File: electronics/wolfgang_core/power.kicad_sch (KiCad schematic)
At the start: 42 parts, among them J1 Power Supply, J2 Battery, Q1 SUM110P06-08L-E3, Q2 SUM110P06-08L-E3, Q3 SUM110P06-08L-E3, Q4 SUM110P06-08L-E3, U1 LM5001MA, U2 ACS724xLCTR-50AB, U3 LTC4418IUF-PBF

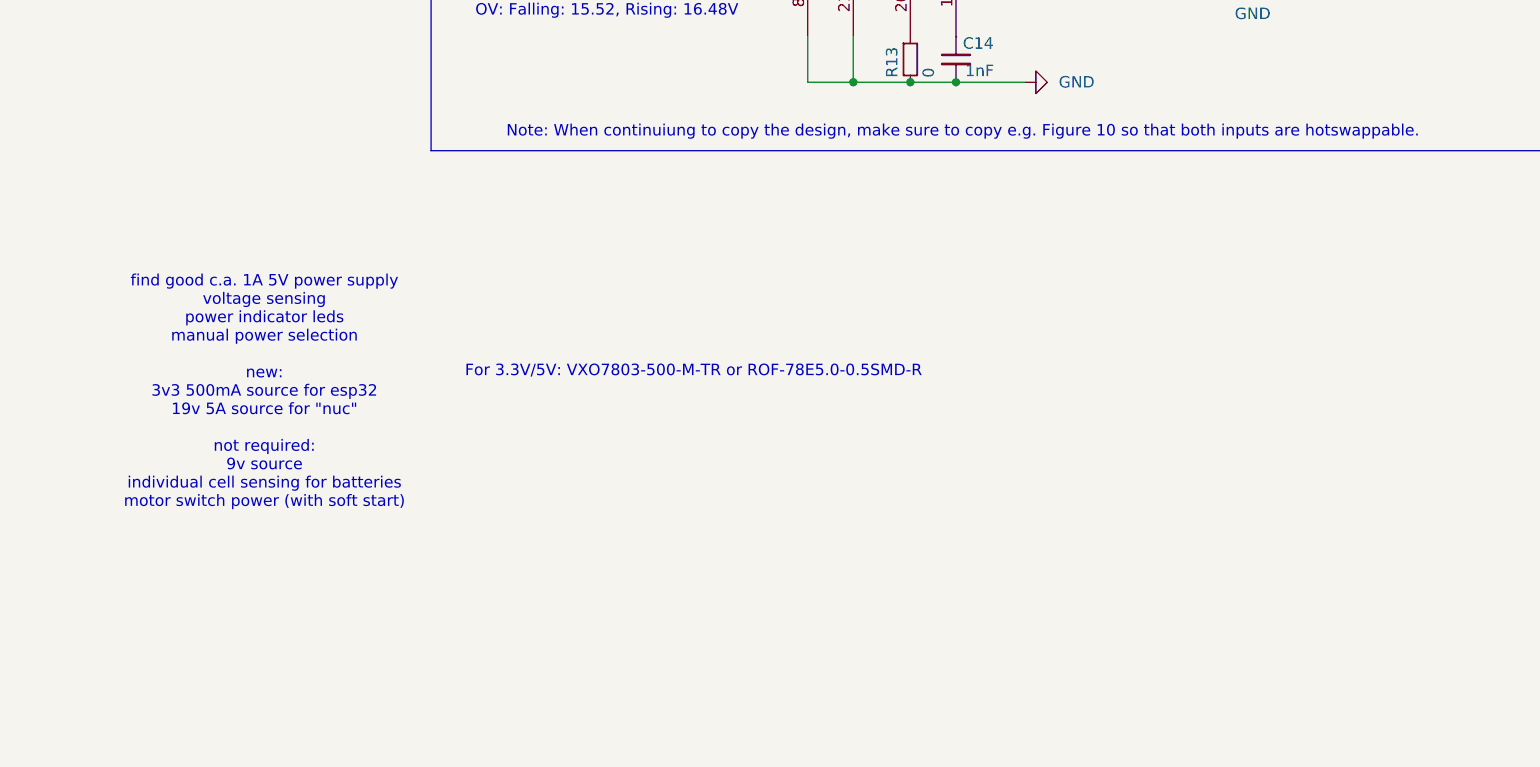
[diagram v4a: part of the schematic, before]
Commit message: Added 5V and 3.3V converters
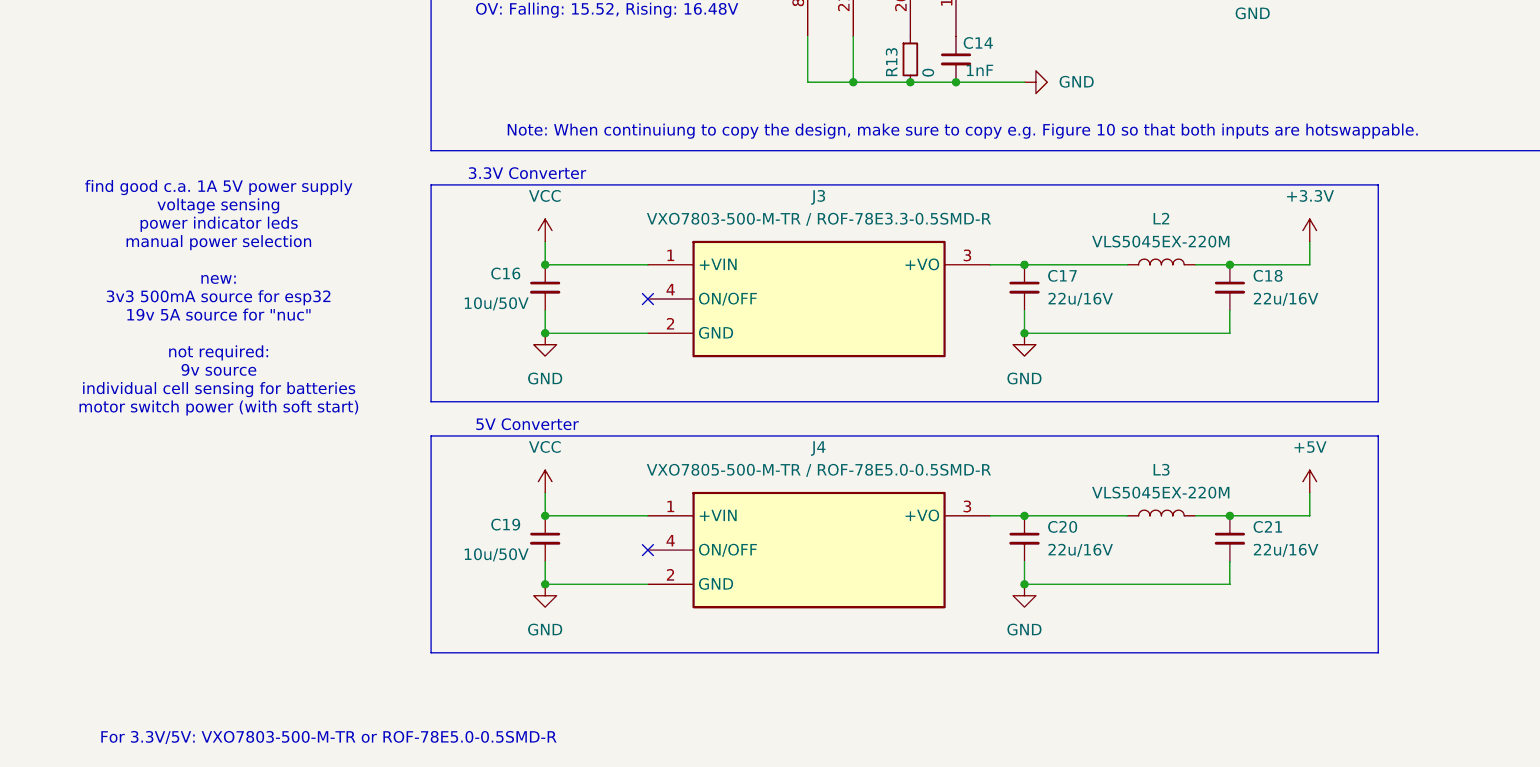
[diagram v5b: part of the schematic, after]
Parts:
- added C16, C19: 10u/50V, symbol Device:C_Small
- added C17, C18, C20, C21: 22u/16V, symbol Device:C_Small
- added J3: VXO7803-500-M-TR / ROF-78E3.3-0.5SMD-R, VXO7803500MTR, symbol VXO7803-500-M-TR:VXO7803-500-M-TR
- added J4: VXO7805-500-M-TR / ROF-78E5.0-0.5SMD-R, VXO7803500MTR, symbol VXO7803-500-M-TR:VXO7803-500-M-TR
- added L2, L3: VLS5045EX-220M, symbol Device:L
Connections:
- net +3.3V: now also C18.1, L2.2
- net +5V: now also C21.1, L3.2
- net GND: now also C16.2, C17.2, C18.2, C19.2, C20.2, C21.2, J3.2 (GND), J4.2 (GND)
- net VCC: now also C16.1, C19.1, J3.1 (+VIN), J4.1 (+VIN)
- new net: C20.1, J4.3 (+VO), L3.1
- new net: C17.1, J3.3 (+VO), L2.1
- no-connect marks 2 -> 4
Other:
- note added: "3.3V Converter"
- note added: "5V Converter"

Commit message: Add Power Switch, Sensing, Indicators
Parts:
- added C23: 0.01uF, symbol Device:C_Small
- added D10: LED RED, symbol Device:LED
- added D11: LED GREEN, symbol Device:LED
- added JP3: bypass uC, symbol Jumper:Jumper_2_Bridged
- added Q5: BSS138P,215, Package_TO_SOT_SMD:SOT-23, symbol Transistor_FET:BSS138
- added Q6: IPD068P03L3GATMA1, symbol Simulation_SPICE:PMOS
- added R14, R18, R21, R23, R25, R27: 10K, symbol Device:R_Small
- added R15: 1K8, symbol Device:R_Small
- added R16: 3K3, symbol Device:R_Small
- added R17: 120, symbol Device:R_Small
- added R19, R29, R30: 4K7, symbol Device:R_Small
- added R20: 100K, symbol Device:R_Small
- added R22, R24, R26, R28: 2K, symbol Device:R_Small
- added SW1: power_switch, symbol Switch:SW_SPDT
- added U4: SN74AHCT1G08, Package_TO_SOT_SMD:SOT-23-5, symbol 74xGxx:74AHCT1G08
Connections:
- net +5V: now also R14.1, R15.1, U4.5 (VCC)
- net GND: now also Q5.2 (S), R16.2, R18.1, R22.2, R24.2, R26.2, R28.2, R29.2, R30.2, SW1.2 (B), U4.3 (GND)
- net VCC: now also D10.2 (A), Q6.3 (S), R19.2, R25.1
- net v_bat: now also R23.1
- net v_ext: now also R21.1
- new net: JP3.2 (B), R15.2, R16.1, U4.2
- new net: Q5.1 (G), R17.2, R18.2
- new net: C23.1, Q6.2 (G), R20.1
- new net: D10.1 (K), R29.1
- new net: Q5.3 (D), R19.1, R20.2
- new net: D11.1 (K), R30.1
- new net VDXL: C23.2, Q6.1 (D)
- new net VXDL: D11.2 (A), R27.1
- new net switch_power: R17.1, U4.4
- new net switch_power_manual: R14.2, SW1.1 (A), U4.1
- new net switch_power_uc: JP3.1 (A)
- new net v_bat_sense: R23.2, R24.1
- new net v_ext_sense: R21.2, R22.1
- new net vcc_sense: R25.2, R26.1
- new net vxdl_sense: R27.2, R28.1
- no-connect marks 4 -> 5
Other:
- note added: "Manual Power Switch"
- note added: "Motor Power Manual/uc selection"
- note added: "Motor Power Switch"
- note added: "Power Indicator LEDs"
- note added: "Voltage Sensing"
- note added: "power indicator leds new: 3v3 500mA source for esp32 19v 5A source for "nuc" not required: 9v source individual cell sensing for batteries"
- note removed: "For 3.3V/5V: VXO7803-500-M-TR or ROF-78E5.0-0.5SMD-R"
- note removed: "find good c.a. 1A 5V power supply voltage sensing power indicator leds manual power selection new: 3v3 500mA source for esp32 19v 5A source for "nuc" not required: 9v source individual cell sensing for batteries motor switch power (with soft start)"

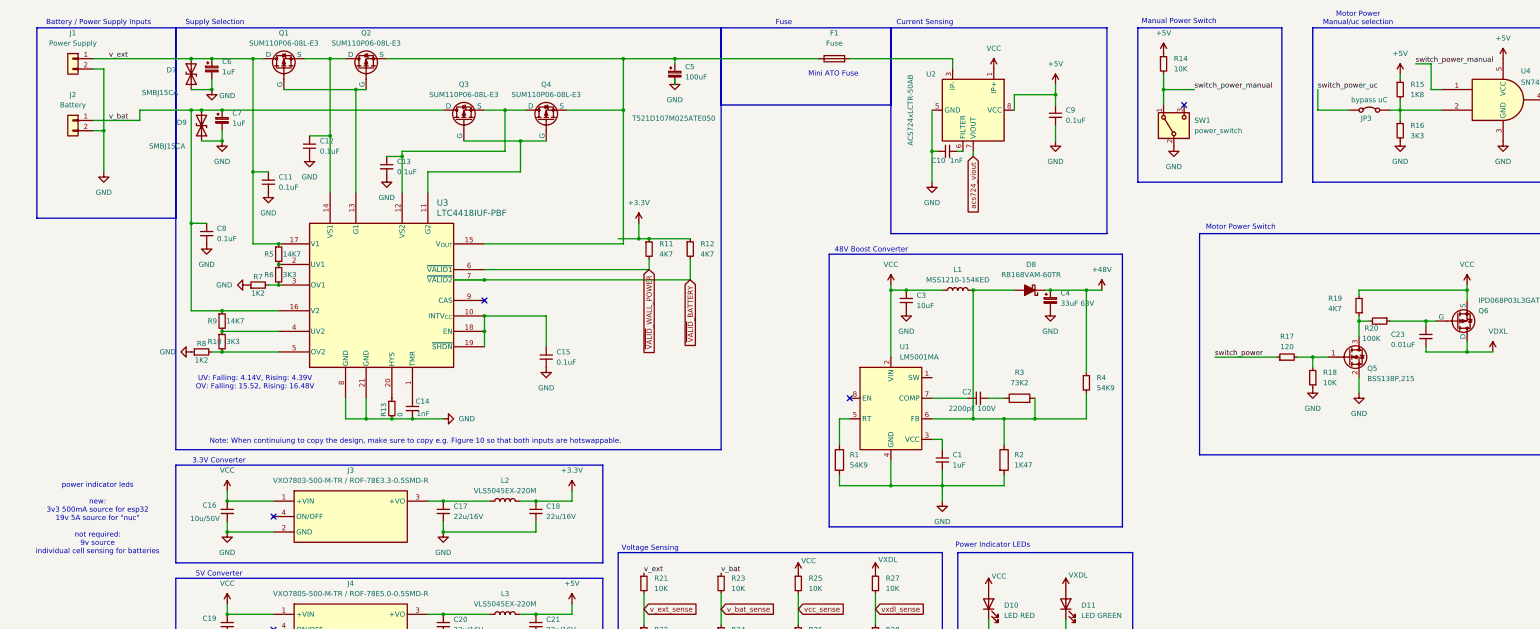
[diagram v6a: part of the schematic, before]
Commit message: Fixup Tranistors directions
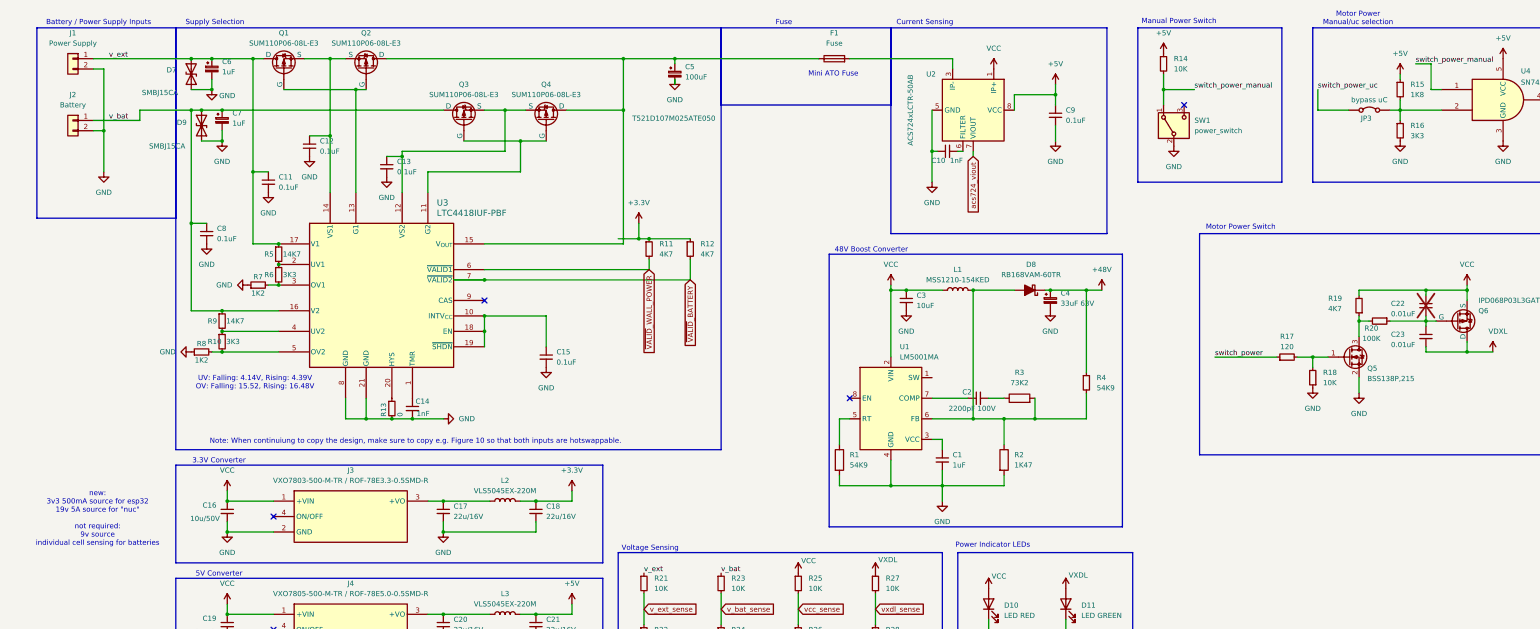
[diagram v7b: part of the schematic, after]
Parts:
- added C22: 0.01uF, symbol Device:C_Small
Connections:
- net VCC: now also C22.1
- net at C23.1, Q6.2 (G), R20.1: now also C22.2
- net at C5.1, F1.1, U3.15 (V_{OUT}): now also Q2.1 (D), Q4.1 (D); no longer Q2.3 (S), Q4.3 (S)
- net at C12.1, Q1.3 (S), U3.14 (VS1): now also Q2.3 (S); no longer Q2.1 (D)
- net at C13.1, Q3.3 (S), U3.12 (VS2): now also Q4.3 (S); no longer Q4.1 (D)
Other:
- note added: "new: 3v3 500mA source for esp32 19v 5A source for "nuc" not required: 9v source individual cell sensing for batteries"
- note removed: "power indicator leds new: 3v3 500mA source for esp32 19v 5A source for "nuc" not required: 9v source individual cell sensing for batteries"
- moved on the sheet: Q2, Q4
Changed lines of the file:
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@@
 	)
 	(junction
+		(at 358.14 82.55)
+		(diameter 0)
+		(color 0 0 0 0)
+	)
+	(junction
 		(at 62.23 170.18)
 		(diameter 0)
@@
 	(wire
 		(pts
+			(xy 358.14 82.55) (xy 358.14 83.82)
+		)
+		(stroke
+			(width 0)
+			(type default)
+		)
+	)
+	(wire
+		(pts
 			(xy 125.73 80.01) (xy 176.53 80.01)
 		)
@@
 	(wire
 		(pts
-			(xy 341.63 82.55) (xy 368.3 82.55)
+			(xy 341.63 82.55) (xy 358.14 82.55)
 		)
 		(stroke
@@
 	(wire
 		(pts
+			(xy 358.14 82.55) (xy 368.3 82.55)
+		)
+		(stroke
+			(width 0)
+			(type default)
+		)
+	)
+	(wire
+		(pts
 			(xy 115.57 139.7) (xy 115.57 142.24)
 		)
@@
 	(wire
 		(pts
+			(xy 358.14 88.9) (xy 358.14 90.17)
+		)
+		(stroke
+			(width 0)
+			(type default)
+		)
+	)
+	(wire
+		(pts
 			(xy 125.73 92.71) (xy 125.73 96.52)
 		)
@@
 		)
 	)
-	(text "power indicator leds\n\nnew:\n3v3 500mA source for esp32\n19v 5A source for \"nuc\"\n\nnot required:\n9v source\nindividual cell sensing for batteries"
+	(text "new:\n3v3 500mA source for esp32\n19v 5A source for \"nuc\"\n\nnot required:\n9v source\nindividual cell sensing for batteries"
 		(exclude_from_sim no)
 		(at 30.226 138.938 0)
@@
 	(symbol
 		(lib_id "Simulation_SPICE:PMOS")
-		(at 140.97 40.64 90)
+		(at 140.97 40.64 270)
+		(mirror x)
 		(unit 1)
 		(exclude_from_sim no)
@@
 		(on_board yes)
 		(dnp no)
-		(fields_autoplaced yes)
 		(property "Reference" "Q4"
 			(at 140.97 31.75 90)
@@
 		)
 		(property "Footprint" ""
-			(at 138.43 35.56 0)
+			(at 143.51 35.56 0)
 			(effects
 				(font
@@
 		)
 		(property "Datasheet" "https://ngspice.sourceforge.io/docs/ngspice-html-manual/manual.xhtml#cha_MOSFETs"
-			(at 153.67 40.64 0)
+			(at 128.27 40.64 0)
 			(effects
 				(font
@@
 		)
 		(property "Sim.Device" "PMOS"
-			(at 158.115 40.64 0)
+			(at 123.825 40.64 0)
 			(effects
 				(font
@@
 		)
 		(property "Sim.Type" "VDMOS"
-			(at 160.02 40.64 0)
+			(at 121.92 40.64 0)
 			(effects
 				(font
@@
 		)
 		(property "Sim.Pins" "1=D 2=G 3=S"
-			(at 156.21 40.64 0)
+			(at 125.73 40.64 0)
 			(effects
 				(font
@@
 	(symbol
 		(lib_id "Simulation_SPICE:PMOS")
-		(at 96.52 27.94 90)
+		(at 96.52 27.94 270)
+		(mirror x)
 		(unit 1)
 		(exclude_from_sim no)
@@
 		(on_board yes)
 		(dnp no)
-		(fields_autoplaced yes)
 		(property "Reference" "Q2"
 			(at 96.52 19.05 90)
@@
 		)
 		(property "Footprint" ""
-			(at 93.98 22.86 0)
+			(at 99.06 22.86 0)
 			(effects
 				(font
@@
 		)
 		(property "Datasheet" "https://ngspice.sourceforge.io/docs/ngspice-html-manual/manual.xhtml#cha_MOSFETs"
-			(at 109.22 27.94 0)
+			(at 83.82 27.94 0)
 			(effects
 				(font
@@
 		)
 		(property "Sim.Device" "PMOS"
-			(at 113.665 27.94 0)
+			(at 79.375 27.94 0)
 			(effects
 				(font
@@
 		)
 		(property "Sim.Type" "VDMOS"
-			(at 115.57 27.94 0)
+			(at 77.47 27.94 0)
 			(effects
 				(font
@@
 		)
 		(property "Sim.Pins" "1=D 2=G 3=S"
-			(at 111.76 27.94 0)
+			(at 81.28 27.94 0)
 			(effects
 				(font
@@
 					(unit 1)
 				)
+			)
+		)
+	)
+	(symbol
+		(lib_id "Device:C_Small")
+		(at 358.14 86.36 0)
+		(unit 1)
+		(exclude_from_sim no)
+		(in_bom yes)
+		(on_board yes)
+		(dnp yes)
+		(property "Reference" "C22"
+			(at 349.504 85.852 0)
+			(effects
+				(font
+					(size 1.27 1.27)
+				)
+				(justify left)
+			)
+		)
+		(property "Value" "0.01uF"
+			(at 349.504 88.392 0)
+			(effects
+				(font
+					(size 1.27 1.27)
+				)
+				(justify left)
+			)
+		)
+		(property "Footprint" ""
+			(at 358.14 86.36 0)
+			(effects
+				(font
+					(size 1.27 1.27)
+				)
+				(hide yes)
+			)
+		)
+		(property "Datasheet" "~"
+			(at 358.14 86.36 0)
+			(effects
+				(font
+					(size 1.27 1.27)
+				)
+				(hide yes)
+			)
+		)
+		(property "Description" "Unpolarized capacitor, small symbol"
+			(at 358.14 86.36 0)
+			(effects
+				(font
+					(size 1.27 1.27)
+				)
+				(hide yes)
+			)
+		)
+		(pin "1"
+		)
+		(pin "2"
+		)
+		(instances
+			(project "wolfgang_core"
+				(path "/9538e4ed-27e6-4c37-b989-9859dc0d49e8/03085433-09a6-46e6-a151-340cb0e29306"
+					(reference "C22")
+					(unit 1)
+				)

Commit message: Edited notes
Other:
- note added: "Options for 19V power supply: (basedd on Texas Instruments WEBENCH) - TPS43061 or TPS43060 (or similar. Some of these seem to not require an external mosfet) - LM3488 or LM3481 (large enough to be hand soldered, but requires external mosfet) - A few members of the LM515 series"
- note added: "new: 3v3 500mA source for esp32 19v 5A source for "nuc" ltc4418 based supply selection soft start on power switch not required: 9v source individual cell sensing for batteries"
- note removed: "new: 3v3 500mA source for esp32 19v 5A source for "nuc" not required: 9v source individual cell sensing for batteries"
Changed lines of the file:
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@@
 		)
 	)
-	(text "new:\n3v3 500mA source for esp32\n19v 5A source for \"nuc\"\n\nnot required:\n9v source\nindividual cell sensing for batteries"
+	(text "new:\n3v3 500mA source for esp32\n19v 5A source for \"nuc\"\nltc4418 based supply selection\nsoft start on power switch\n\nnot required:\n9v source\nindividual cell sensing for batteries"
 		(exclude_from_sim no)
 		(at 30.226 138.938 0)
@@
 		)
 	)
+	(text "Options for 19V power supply: (basedd on Texas Instruments WEBENCH)\n- TPS43061 or TPS43060 (or similar. Some of these seem to not require an external mosfet)\n- LM3488 or LM3481 (large enough to be hand soldered, but requires external mosfet)\n- A few members of the LM515 series"
+		(exclude_from_sim no)
+		(at 14.478 193.548 0)
+		(effects
+			(font
+				(size 1.27 1.27)
+			)
+			(justify left)
+		)
+	)
